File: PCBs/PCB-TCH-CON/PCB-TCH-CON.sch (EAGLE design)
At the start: 13 parts

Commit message: asdf
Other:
- note added: "Pin 1 of the 7-wire menu cable on the Touch Screen Controller board is the wire CLOSEST to the flatcable connecting the Controller board with the panel. And IDC Connector (8W) is crimped onto these 7 wires and connected to TSCABLE."
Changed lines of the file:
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@@
 <text x="55.88" y="43.18" size="2.54" layer="97">TOUCH</text>
 <text x="55.88" y="2.54" size="1.778" layer="97">EXTRA POWER (Vin)</text>
+<text x="-53.34" y="-17.78" size="1.778" layer="97">Pin 1 of the 7-wire menu cable on the Touch Screen Controller board
+is the wire CLOSEST to the flatcable connecting the Controller board with the panel.
+And IDC Connector (8W) is crimped onto these 7 wires and connected to TSCABLE.</text>
 </plain>
 <instances>
@@
 </schematic>
 </drawing>
+<compatibility>
+<note version="6.3" minversion="6.2.2" severity="warning">
+Since Version 6.2.2 text objects can contain more than one line,
+which will not be processed correctly with this version.
+</note>
+</compatibility>
 </eagle>

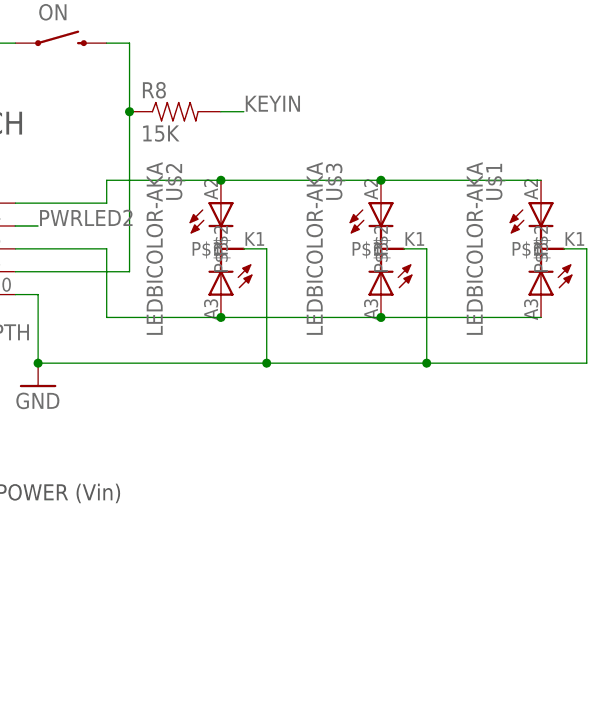
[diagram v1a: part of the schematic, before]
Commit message: Large revisions of boards, change of forms, in particular all mounting holes now has a 7mm diameter and fully inside the board.
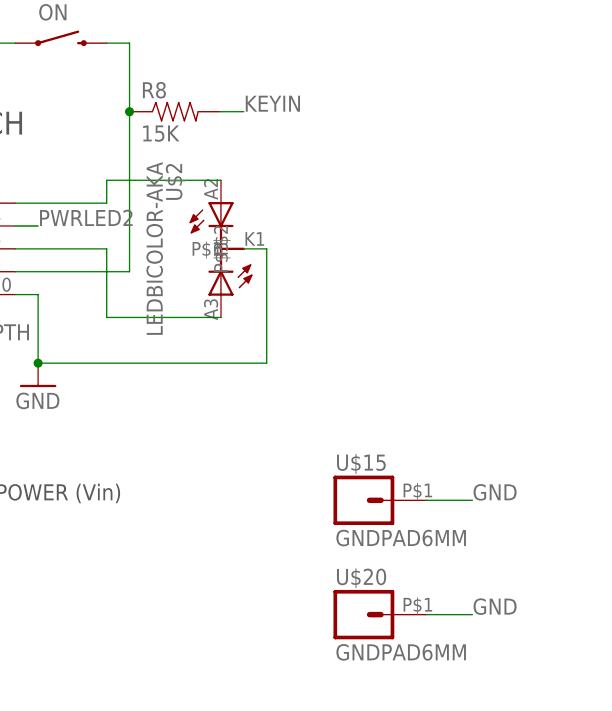
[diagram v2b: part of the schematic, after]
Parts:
- removed U$1, U$3: LEDBICOLOR-AKA, SKAARHOJ:LEDBICOLOR-AKA
- added U$15, U$20: GNDPAD6MM, SKAARHOJ:GNDPAD6MM
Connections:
- net GND: now also U$15.1, U$20.1; no longer U$1.P$1, U$3.P$1
- net N$1: no longer U$1.P$2, U$3.P$2
- net N$2: no longer U$1.P$3, U$3.P$3
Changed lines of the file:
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@@
 </class>
 <class number="1" name="Power" width="0.4064" drill="0.6096">
-<clearance class="1" value="0.3048"/>
+<clearance class="1" value="0.2032"/>
 </class>
 </classes>
@@
 <part name="GND3" library="SparkFun" deviceset="GND" device=""/>
 <part name="R8" library="SparkFun" deviceset="RESISTOR" device="0603-RES" value="15K"/>
-<part name="U$3" library="SKAARHOJ" deviceset="LEDBICOLOR-AKA" device=""/>
-<part name="U$1" library="SKAARHOJ" deviceset="LEDBICOLOR-AKA" device=""/>
 <part name="TSCABLE1" library="SparkFun" deviceset="M04X2" device=""/>
 <part name="SRC" library="SparkFun" deviceset="SWITCH-MOMENTARY-2" device=""/>
@@
 <part name="ON" library="SparkFun" deviceset="SWITCH-MOMENTARY-2" device=""/>
 <part name="R2" library="SparkFun" deviceset="RESISTOR" device="0603-RES" value="1K"/>
+<part name="U$15" library="SKAARHOJ" deviceset="GNDPAD" device="6MM" value="GNDPAD6MM"/>
+<part name="U$20" library="SKAARHOJ" deviceset="GNDPAD" device="6MM" value="GNDPAD6MM"/>
 </parts>
 <sheets>
@@
 <instance part="GND3" gate="1" x="38.1" y="-5.08"/>
 <instance part="R8" gate="G$1" x="83.82" y="45.72"/>
-<instance part="U$3" gate="G$1" x="106.68" y="30.48"/>
-<instance part="U$1" gate="G$1" x="124.46" y="30.48"/>
 <instance part="TSCABLE1" gate="G$1" x="-40.64" y="30.48"/>
 <instance part="SRC" gate="G$1" x="71.12" y="63.5" smashed="yes">
@@
 </instance>
 <instance part="R2" gate="G$1" x="7.62" y="60.96"/>
+<instance part="U$15" gate="G$1" x="106.68" y="2.54"/>
+<instance part="U$20" gate="G$1" x="106.68" y="-10.16"/>
 </instances>
 <busses>
@@
 <wire x1="93.98" y1="17.78" x2="68.58" y2="17.78" width="0.1524" layer="91"/>
 <junction x="68.58" y="17.78"/>
-<pinref part="U$3" gate="G$1" pin="P$1"/>
-<wire x1="109.22" y1="30.48" x2="111.76" y2="30.48" width="0.1524" layer="91"/>
-<wire x1="111.76" y1="30.48" x2="111.76" y2="17.78" width="0.1524" layer="91"/>
-<wire x1="111.76" y1="17.78" x2="93.98" y2="17.78" width="0.1524" layer="91"/>
-<junction x="93.98" y="17.78"/>
-<pinref part="U$1" gate="G$1" pin="P$1"/>
-<wire x1="127" y1="30.48" x2="129.54" y2="30.48" width="0.1524" layer="91"/>
-<wire x1="129.54" y1="30.48" x2="129.54" y2="17.78" width="0.1524" layer="91"/>
-<wire x1="129.54" y1="17.78" x2="111.76" y2="17.78" width="0.1524" layer="91"/>
-<junction x="111.76" y="17.78"/>
 </segment>
 <segment>
@@
 <wire x1="66.04" y1="53.34" x2="63.5" y2="53.34" width="0.1524" layer="91"/>
 <label x="63.5" y="53.34" size="1.778" layer="95" rot="R180"/>
+</segment>
+<segment>
+<pinref part="U$15" gate="G$1" pin="1"/>
+<wire x1="111.76" y1="2.54" x2="116.84" y2="2.54" width="0.1524" layer="91"/>
+<label x="116.84" y="2.54" size="1.778" layer="95"/>
+</segment>
+<segment>
+<pinref part="U$20" gate="G$1" pin="1"/>
+<wire x1="111.76" y1="-10.16" x2="116.84" y2="-10.16" width="0.1524" layer="91"/>
+<label x="116.84" y="-10.16" size="1.778" layer="95"/>
 </segment>
 </net>
@@
 <pinref part="U$2" gate="G$1" pin="P$2"/>
 <wire x1="76.2" y1="38.1" x2="88.9" y2="38.1" width="0.1524" layer="91"/>
-<pinref part="U$3" gate="G$1" pin="P$2"/>
-<wire x1="106.68" y1="38.1" x2="88.9" y2="38.1" width="0.1524" layer="91"/>
-<junction x="88.9" y="38.1"/>
-<pinref part="U$1" gate="G$1" pin="P$2"/>
-<wire x1="106.68" y1="38.1" x2="124.46" y2="38.1" width="0.1524" layer="91"/>
-<junction x="106.68" y="38.1"/>
 </segment>
 </net>
@@
 <pinref part="U$2" gate="G$1" pin="P$3"/>
 <wire x1="76.2" y1="22.86" x2="88.9" y2="22.86" width="0.1524" layer="91"/>
-<pinref part="U$3" gate="G$1" pin="P$3"/>
-<wire x1="88.9" y1="22.86" x2="106.68" y2="22.86" width="0.1524" layer="91"/>
-<junction x="88.9" y="22.86"/>
-<pinref part="U$1" gate="G$1" pin="P$3"/>
-<wire x1="124.46" y1="22.86" x2="106.68" y2="22.86" width="0.1524" layer="91"/>
-<junction x="106.68" y="22.86"/>
-</segment>
-</net>
+</segment>
+</net>

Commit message: Various changes
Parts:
- added C1: 100n, SmartPrj:C-EU0603-RND
- added PC1: 47u, rcl:CPOL-EUD
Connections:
- net GND: now also C1.2, PC1.-
- net VIN: now also C1.1, PC1.+
